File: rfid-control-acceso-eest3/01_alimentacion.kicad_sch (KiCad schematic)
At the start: 11 parts, among them J1 BOARD_12VDC_2.5A, J2 BUCK?

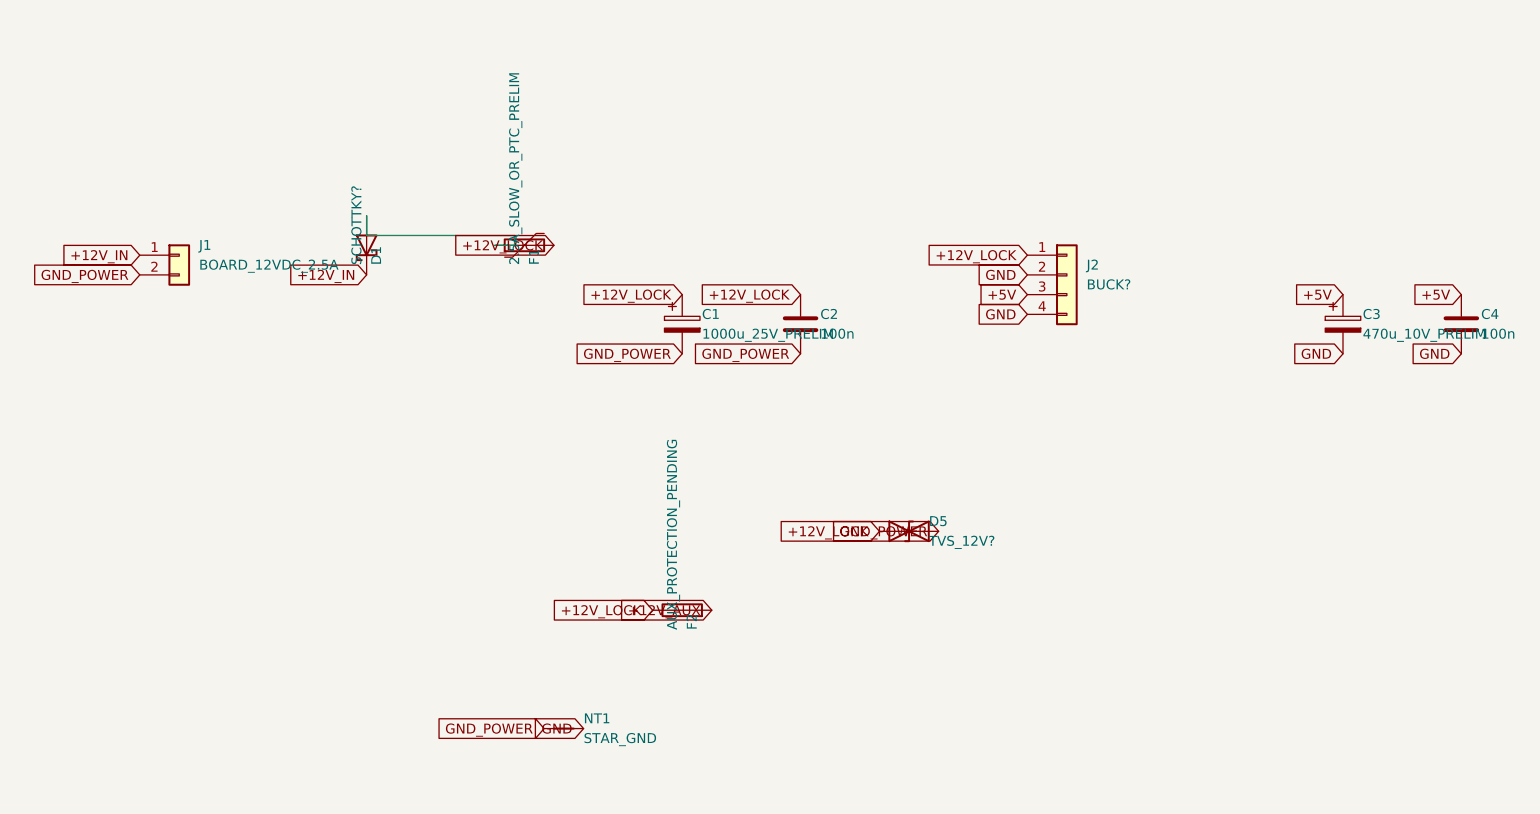
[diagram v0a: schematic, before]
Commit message: Reorganiza floorplan PCB Rev A antes del ruteo
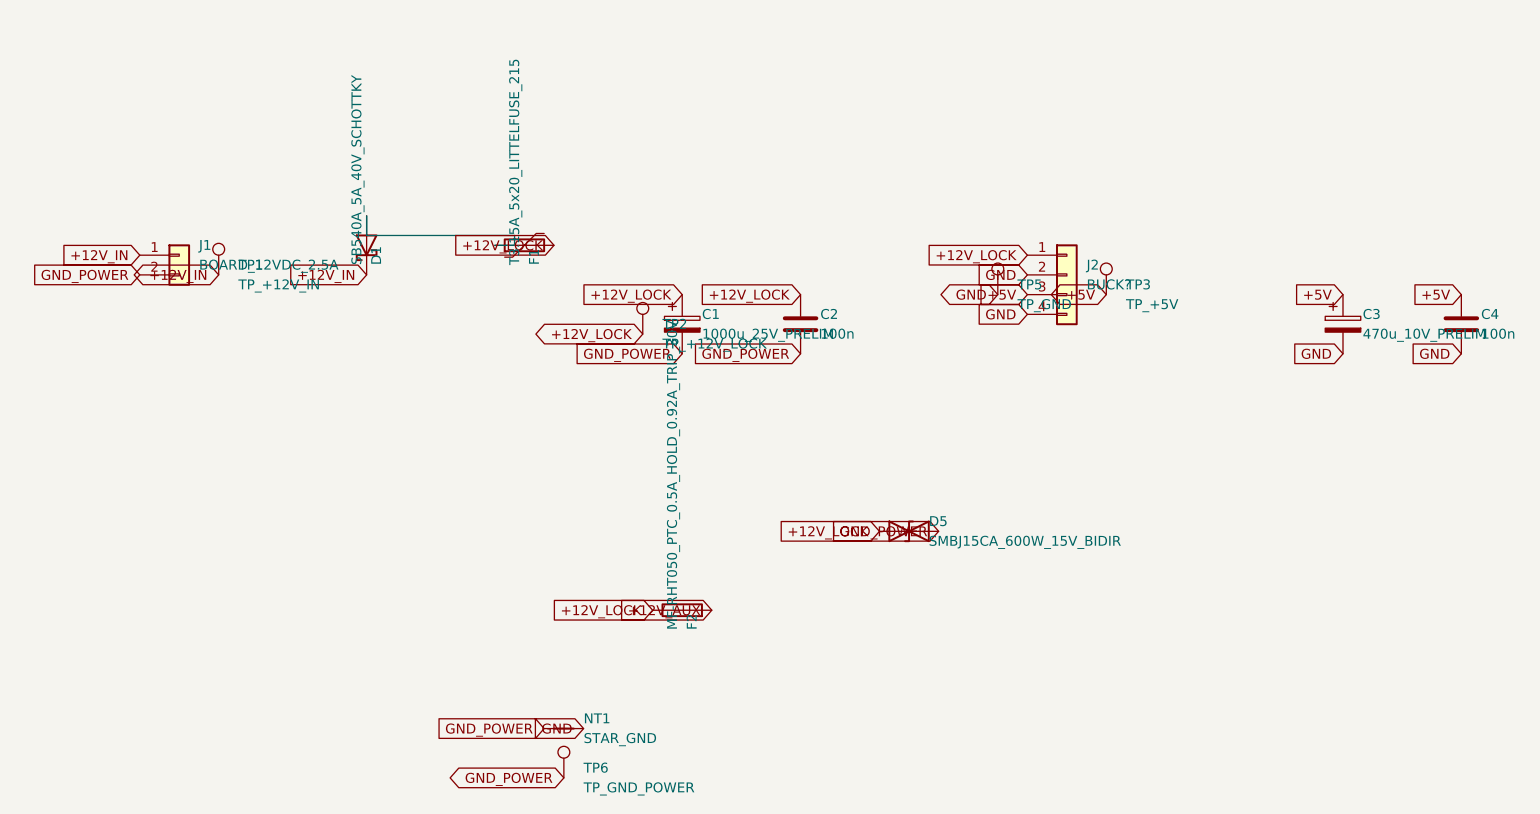
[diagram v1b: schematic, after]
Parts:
- added TP1: TP_+12V_IN, TestPoint:TestPoint_THTPad_D2.0mm_Drill1.0mm, symbol Connector:TestPoint
- added TP2: TP_+12V_LOCK, TestPoint:TestPoint_THTPad_D2.0mm_Drill1.0mm, symbol Connector:TestPoint
- added TP3: TP_+5V, TestPoint:TestPoint_THTPad_D2.0mm_Drill1.0mm, symbol Connector:TestPoint
- added TP5: TP_GND, TestPoint:TestPoint_THTPad_D2.0mm_Drill1.0mm, symbol Connector:TestPoint
- added TP6: TP_GND_POWER, TestPoint:TestPoint_THTPad_D2.0mm_Drill1.0mm, symbol Connector:TestPoint
- C1: footprint (none) -> rfid_eest3:CP_Radial_D16_P7.50_PLACEHOLDER_NO_FABRICAR
- C2, C4: footprint (none) -> Capacitor_THT:C_Disc_D5.0mm_W2.5mm_P5.00mm
- C3: footprint (none) -> rfid_eest3:CP_Radial_D10_P5.00_PLACEHOLDER_NO_FABRICAR
- D1: value SCHOTTKY? -> SB540A_5A_40V_SCHOTTKY; footprint (none) -> Diode_THT:D_DO-201AD_P15.24mm_Horizontal; MPN (none) -> SB540A-E3/54; Manufacturer (none) -> Vishay
- D5: value TVS_12V? -> SMBJ15CA_600W_15V_BIDIR; footprint (none) -> Diode_SMD:D_SMB; MPN (none) -> SMBJ15CA; Manufacturer (none) -> Littelfuse
- F1: value 2.5A_SLOW_OR_PTC_PRELIM -> T3.15A_5x20_LITTELFUSE_215; footprint (none) -> Fuse:Fuseholder_Clip-5x20mm_Bel_FC-203-22_Lateral_P17.80x5.00mm_D1.17mm_Horizontal; MPN (none) -> 021503.15MXP + FC-203-22; Manufacturer (none) -> Littelfuse + Bel
- F2: value AUX_PROTECTION_PENDING -> MF-RHT050_PTC_0.5A_HOLD_0.92A_TRIP_30V; footprint (none) -> Fuse:Fuse_Bourns_MF-RHT050; MPN (none) -> MF-RHT050; Manufacturer (none) -> Bourns
- J1: footprint (none) -> rfid_eest3:KF301_2P_P5.08_PLACEHOLDER_NO_FABRICAR
- J2: footprint (none) -> rfid_eest3:KF301_4P_P5.08_PLACEHOLDER_NO_FABRICAR
- NT1: footprint (none) -> NetTie:NetTie-2_THT_Pad1.0mm
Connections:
- net +12V_IN: now also TP1.1
- net +12V_LOCK: now also TP2.1
- net +5V: now also TP3.1
- net GND: now also TP5.1
- net GND_POWER: now also TP6.1
